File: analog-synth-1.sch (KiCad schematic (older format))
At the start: 55 parts, among them J1 CONN_02X08, J2 PJ301M-12, J3 PJ301M-12, J4 PJ301M-12, J5 PJ301M-12, Q1 2N3904, Q2 2N3904, Q3 2N3904, Q4 2N3906, Q5 2N3904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

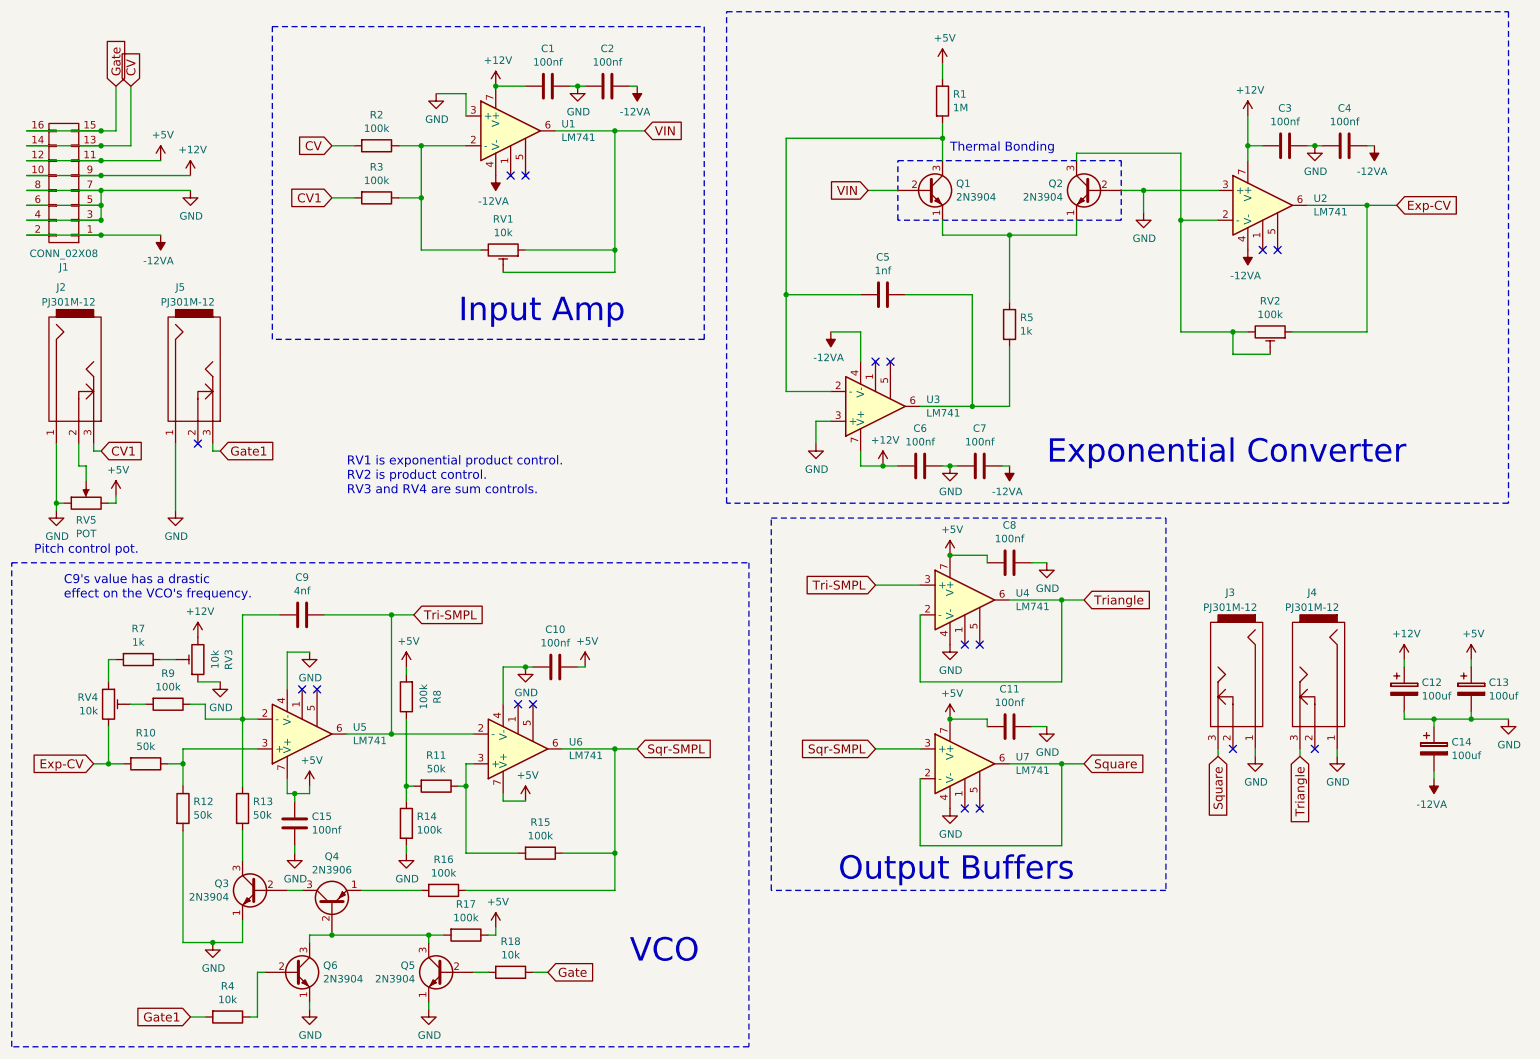
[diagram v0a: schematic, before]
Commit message: Replace 4xLM741 with LM324
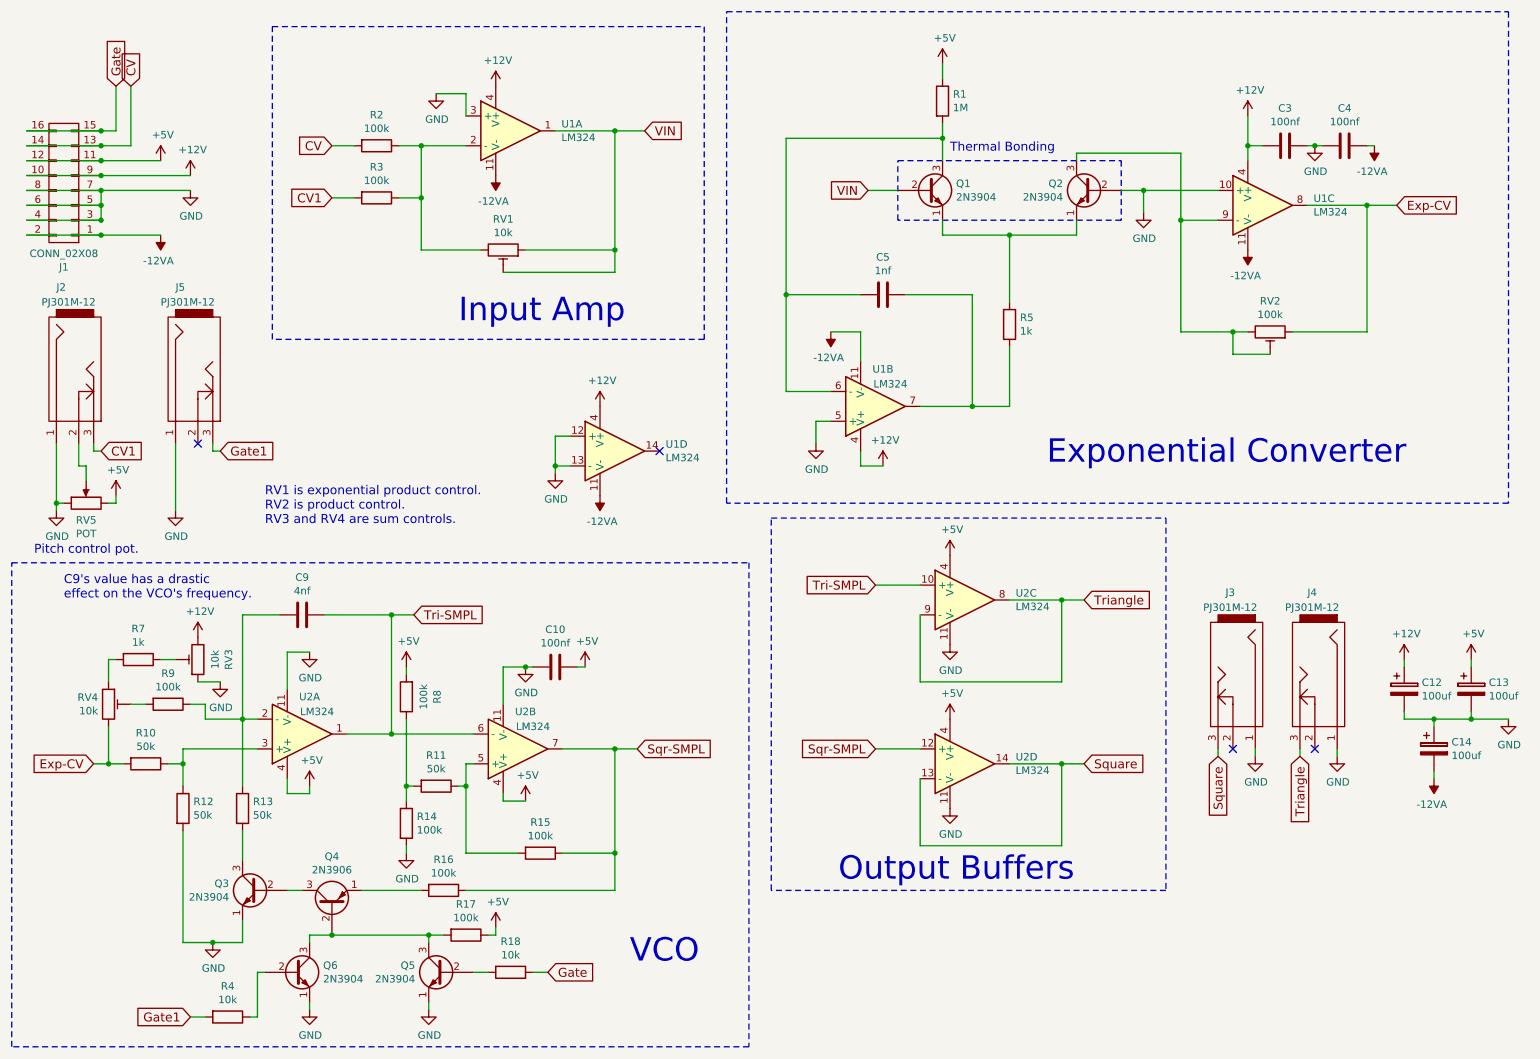
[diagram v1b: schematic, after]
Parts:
- removed C1, C11, C15, C2, C6, C7, C8: 100nf, Capacitors_THT:C_Disc_D5.0mm_W2.5mm_P2.50mm, symbol C
- removed U1, U2, U3, U4, U5, U6, U7: LM741, Housings_DIP:DIP-8_W7.62mm, symbol LM741
- added U1, U2: LM324, symbol LM324
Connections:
- net +12V: now also U1.4 (V+), U1.4 (V+), U1.4 (V+), U1.4 (V+)
- net +5V: now also U2.4 (V+), U2.4 (V+), U2.4 (V+), U2.4 (V+)
- net -12VA: now also U1.11 (V-), U1.11 (V-), U1.11 (V-), U1.11 (V-)
- net Exp-CV: now also U1.8
- net GND: now also U1.10 (+), U1.12 (+), U1.13 (-), U1.3 (+), U1.5 (+), U2.11 (V-), U2.11 (V-), U2.11 (V-), U2.11 (V-)
- net Sqr-SMPL: now also U2.12 (+), U2.7
- net Square: now also U2.13 (-), U2.14
- net Tri-SMPL: now also U2.1, U2.10 (+), U2.6 (-)
- net Triangle: now also U2.8, U2.9 (-)
- net VIN: now also U1.1
- net at R2.1, R3.1, RV1.3: now also U1.2 (-)
- net at C5.2, Q1.3 (C), R1.2: now also U1.6 (-)
- net at C5.1, R5.2: now also U1.7
- net at Q2.3 (C), RV2.2, RV2.3: now also U1.9 (-)
- net at R10.1, R12.1: now also U2.3 (+)
- net at C9.2, R13.1, R9.1: now also U2.2 (-)
- net at R11.1, R15.2: now also U2.5 (+)
- no-connect marks 17 -> 4
